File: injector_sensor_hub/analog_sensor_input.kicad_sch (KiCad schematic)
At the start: 24 parts, among them J3 Conn_01x02_Female-Connector, J4 Conn_01x02_Female-Connector, J5 Conn_01x03_Female, J6 Conn_01x02_Female-Connector, J7 Conn_01x03_Female, J8 Conn_01x02_Female-Connector

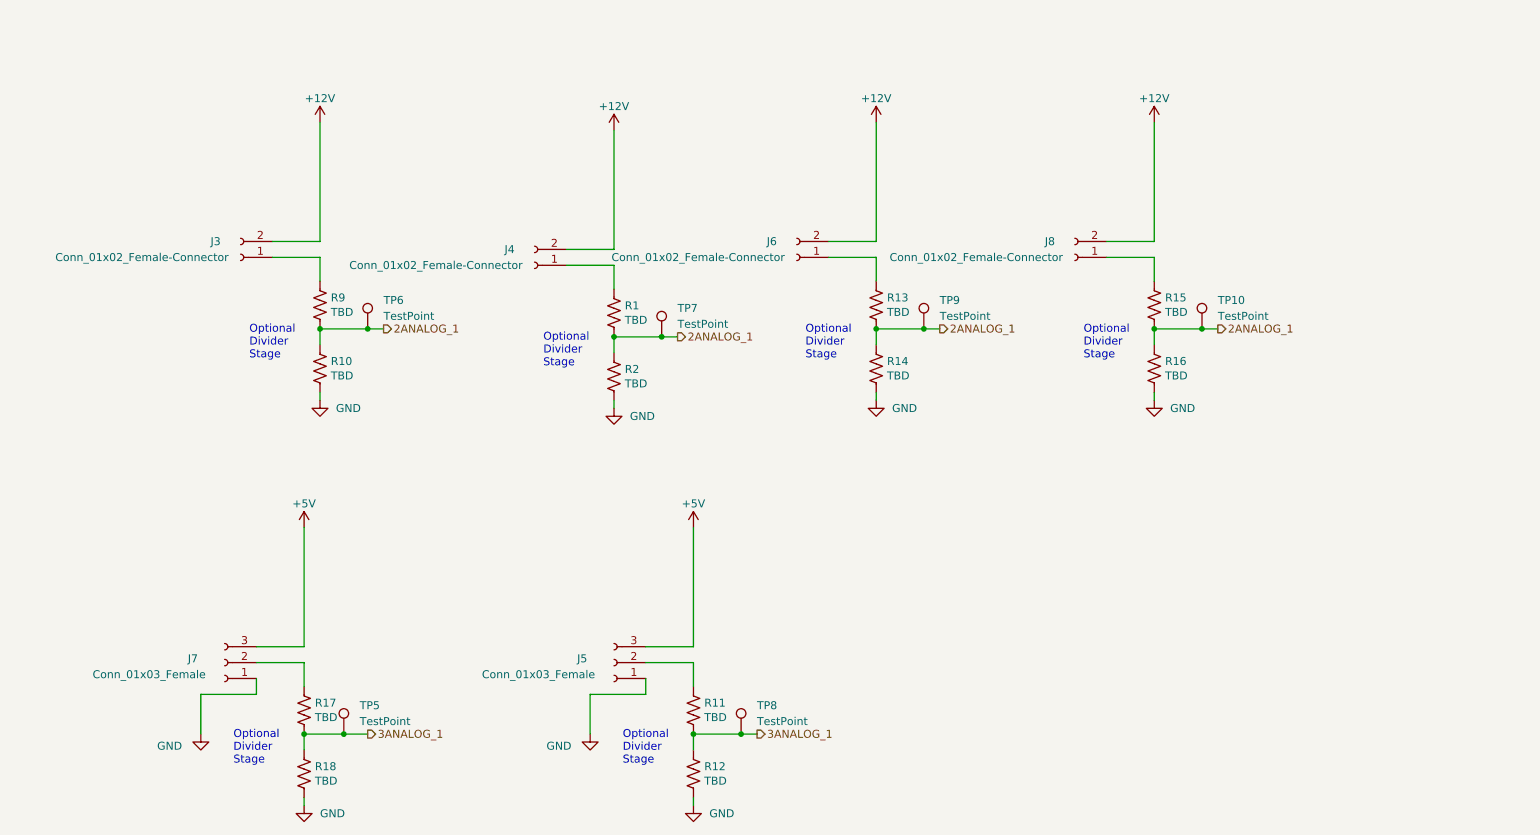
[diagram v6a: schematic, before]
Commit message: fixed sensor count inconsistency
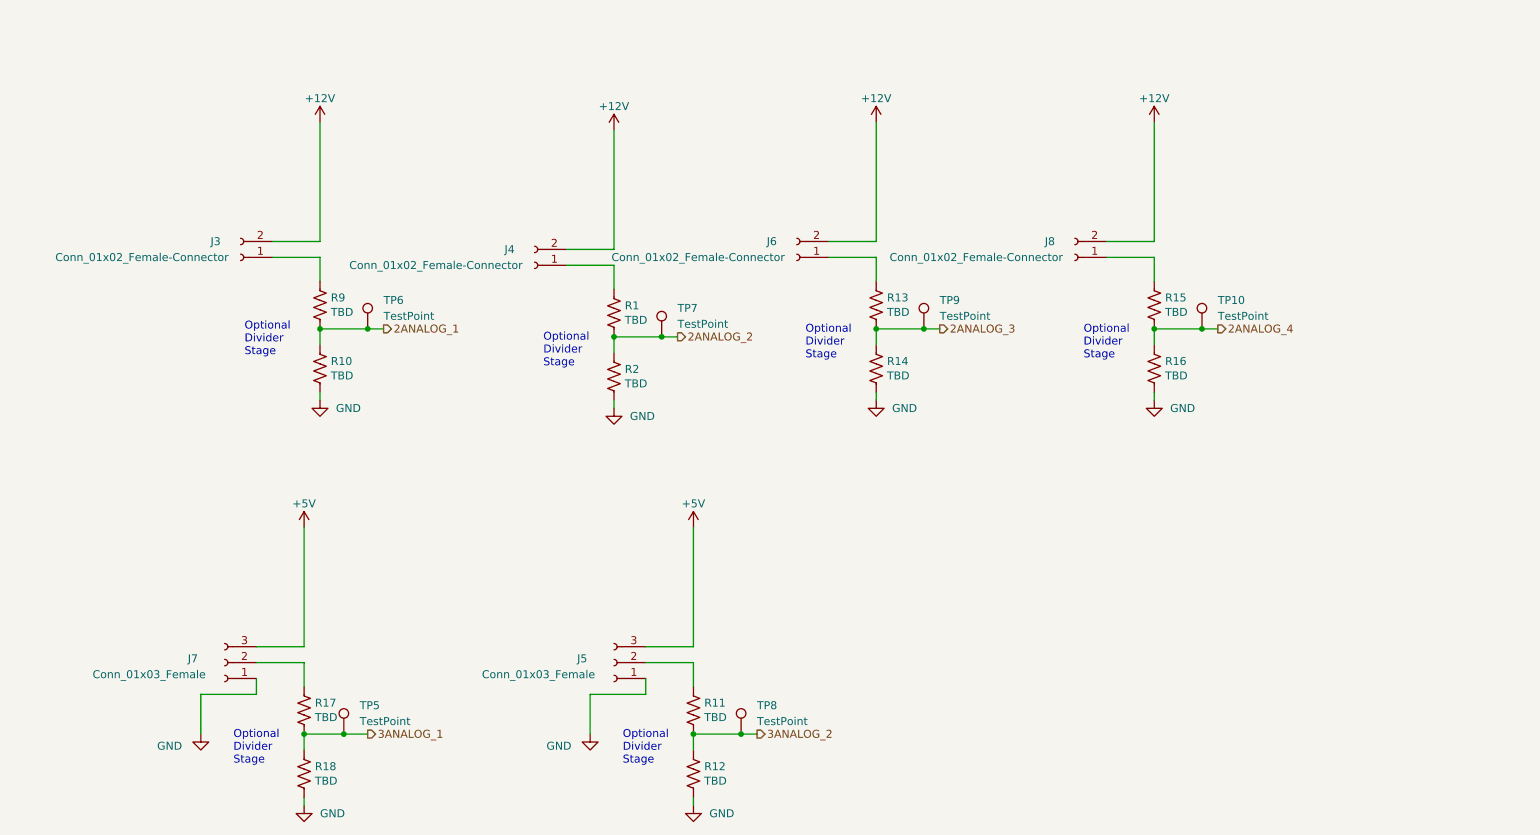
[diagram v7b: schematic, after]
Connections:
- net 2ANALOG_1: no longer R1.2, R13.2, R14.1, R15.2, R16.1, R2.1, TP10.1, TP7.1, TP9.1
- net 3ANALOG_1: no longer R11.2, R12.1, TP8.1
- new net 2ANALOG_2: R1.2, R2.1, TP7.1
- new net 2ANALOG_3: R13.2, R14.1, TP9.1
- new net 2ANALOG_4: R15.2, R16.1, TP10.1
- new net 3ANALOG_2: R11.2, R12.1, TP8.1
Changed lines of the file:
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@@
 	(text "Optional\nDivider \nStage"
 		(exclude_from_sim no)
-		(at 66.167 77.343 0)
+		(at 65.405 76.835 0)
 		(effects
 			(font
@@
 		)
 	)
-	(hierarchical_label "2ANALOG_1"
+	(hierarchical_label "2ANALOG_3"
 		(shape output)
 		(at 176.53 72.39 0)
@@
 		)
 	)
-	(hierarchical_label "2ANALOG_1"
+	(hierarchical_label "2ANALOG_4"
 		(shape output)
 		(at 220.98 72.39 0)
@@
 		)
 	)
-	(hierarchical_label "2ANALOG_1"
+	(hierarchical_label "2ANALOG_2"
 		(shape output)
 		(at 134.62 73.66 0)
@@
 		)
 	)
-	(hierarchical_label "3ANALOG_1"
+	(hierarchical_label "3ANALOG_2"
 		(shape output)
 		(at 147.32 137.16 0)

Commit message: started layout for pcb
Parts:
- TP10, TP5, TP6, TP7, TP8, TP9: footprint (none) -> TestPoint:TestPoint_Pad_D1.5mm
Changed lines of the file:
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@@
 			)
 		)
-		(property "Footprint" ""
+		(property "Footprint" "TestPoint:TestPoint_Pad_D1.5mm"
 			(at 223.52 72.39 0)
 			(effects
@@
 			)
 		)
-		(property "Footprint" ""
+		(property "Footprint" "TestPoint:TestPoint_Pad_D1.5mm"
 			(at 90.17 72.39 0)
 			(effects
@@
 			)
 		)
-		(property "Footprint" ""
+		(property "Footprint" "TestPoint:TestPoint_Pad_D1.5mm"
 			(at 137.16 73.66 0)
 			(effects
@@
 			)
 		)
-		(property "Footprint" ""
+		(property "Footprint" "TestPoint:TestPoint_Pad_D1.5mm"
 			(at 86.36 137.16 0)
 			(effects
@@
 			)
 		)
-		(property "Footprint" ""
+		(property "Footprint" "TestPoint:TestPoint_Pad_D1.5mm"
 			(at 149.86 137.16 0)
 			(effects
@@
 			)
 		)
-		(property "Footprint" ""
+		(property "Footprint" "TestPoint:TestPoint_Pad_D1.5mm"
 			(at 179.07 72.39 0)
 			(effects
